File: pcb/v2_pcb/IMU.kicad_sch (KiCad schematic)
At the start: 13 parts, among them U1000 SCH16T-K01

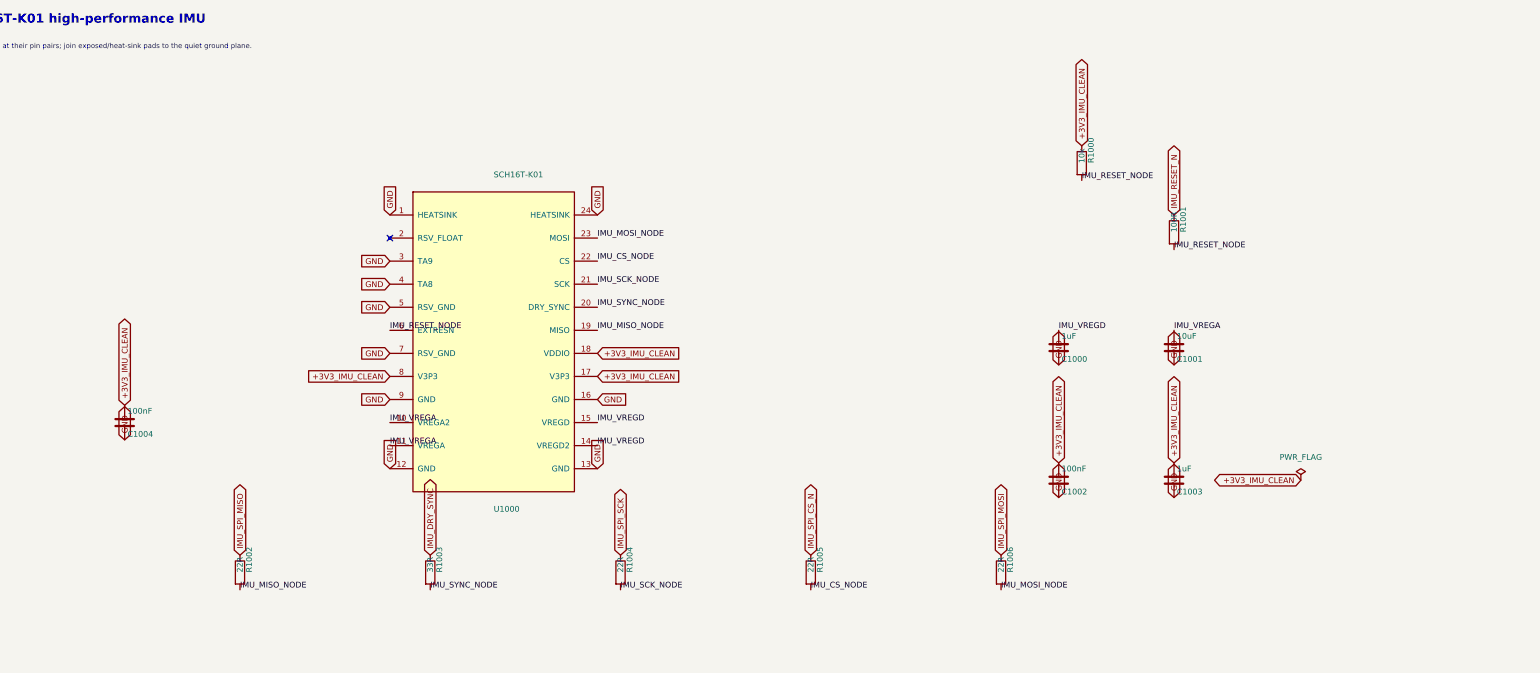
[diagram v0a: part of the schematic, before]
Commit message: switch mosfets
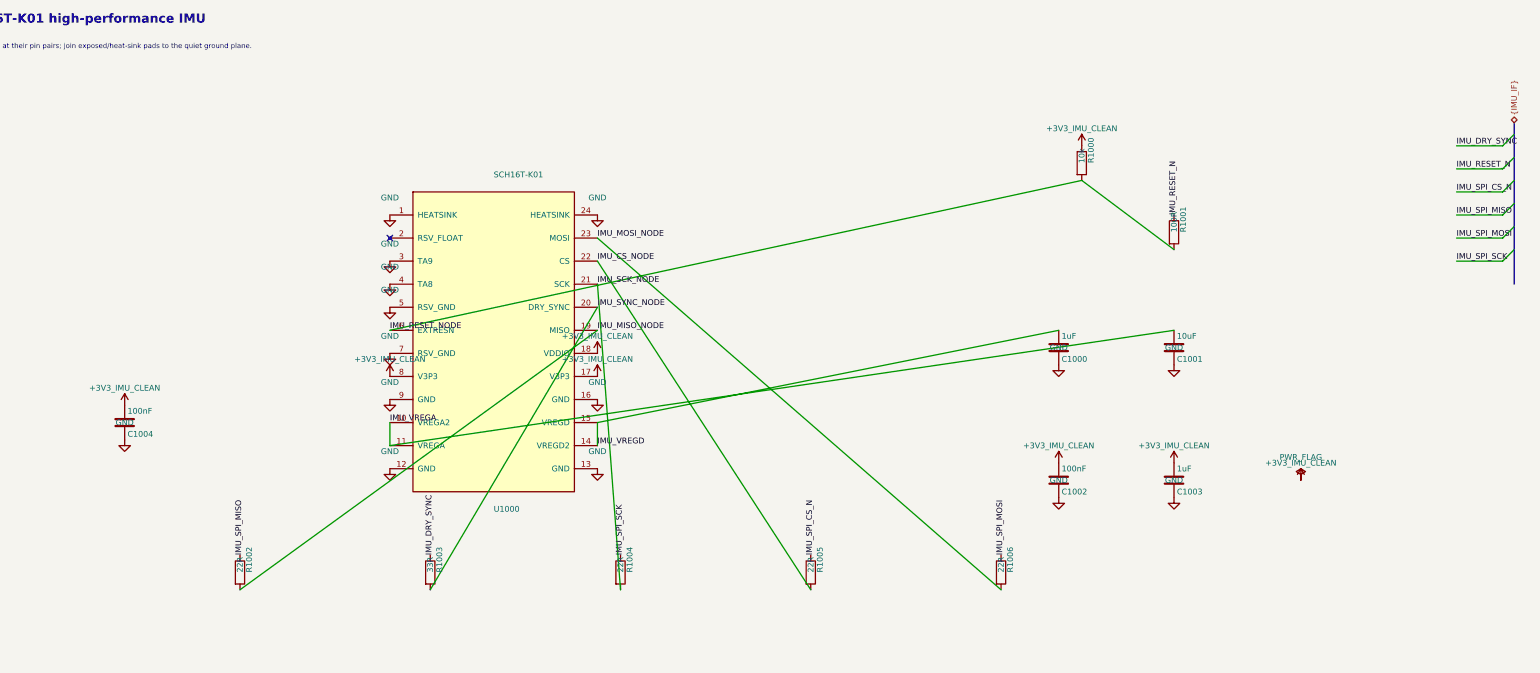
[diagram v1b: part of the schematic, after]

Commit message: clean pcb
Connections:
- net IMU_CS_NODE: no longer names the net of R1005.2, U1000.22 (CS)
- net IMU_MISO_NODE: no longer names the net of R1002.2, U1000.19 (MISO)
- net IMU_MOSI_NODE: no longer names the net of R1006.2, U1000.23 (MOSI)
- net IMU_RESET_NODE: no longer names the net of R1000.2, R1001.2, U1000.6 (EXTRESN)
- net IMU_SCK_NODE: no longer names the net of R1004.2, U1000.21 (SCK)
- net IMU_SYNC_NODE: no longer names the net of R1003.2, U1000.20 (DRY_SYNC)
- net IMU_VREGA: no longer names the net of C1001.1, U1000.10 (VREGA2), U1000.11 (VREGA)
- net IMU_VREGD: no longer names the net of C1000.1, U1000.14 (VREGD2), U1000.15 (VREGD)
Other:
- moved on the sheet: C1000, C1001, C1002, C1003, C1004, R1000, R1001, R1002, R1003, R1004, R1005, R1006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

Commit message: small
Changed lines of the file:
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@@
-	)
-	(junction
-		(at 175.26 127)
-		(diameter 0)
-		(color 0 0 0 0)
 	)
 	(junction
@@
 	)
 	(junction
+		(at 162.56 119.38)
+		(diameter 0)
+		(color 0 0 0 0)
+	)
+	(junction
 		(at 248.92 133.35)
 		(diameter 0)
@@
 	)
 	(junction
+		(at 162.56 127)
+		(diameter 0)
+		(color 0 0 0 0)
+	)
+	(junction
 		(at 191.77 113.03)
 		(diameter 0)
@@
 	(wire
 		(pts
+			(xy 168.91 113.03) (xy 182.88 113.03)
+		)
+		(stroke
+			(width 0)
+			(type default)
+		)
+	)
+	(wire
+		(pts
 			(xy 196.85 97.79) (xy 195.58 97.79)
 		)
@@
 	(wire
 		(pts
+			(xy 241.3 133.35) (xy 248.92 133.35)
+		)
+		(stroke
+			(width 0)
+			(type default)
+		)
+	)
+	(wire
+		(pts
+			(xy 337.82 76.2) (xy 347.98 76.2)
+		)
+		(stroke
+			(width 0)
+			(type default)
+		)
+	)
+	(wire
+		(pts
+			(xy 195.58 123.19) (xy 187.96 123.19)
+		)
+		(stroke
+			(width 0)
+			(type default)
+		)
+	)
+	(wire
+		(pts
+			(xy 256.54 119.38) (xy 267.97 119.38)
+		)
+		(stroke
+			(width 0)
+			(type default)
+		)
+	)
+	(wire
+		(pts
+			(xy 191.77 109.22) (xy 191.77 113.03)
+		)
+		(stroke
+			(width 0)
+			(type default)
+		)
+	)
+	(wire
+		(pts
+			(xy 195.58 133.35) (xy 187.96 133.35)
+		)
+		(stroke
+			(width 0)
+			(type default)
+		)
+	)
+	(wire
+		(pts
 			(xy 162.56 119.38) (xy 175.26 119.38)
-		)
-		(stroke
-			(width 0)
-			(type default)
-		)
-	)
-	(wire
-		(pts
-			(xy 241.3 133.35) (xy 248.92 133.35)
-		)
-		(stroke
-			(width 0)
-			(type default)
-		)
-	)
-	(wire
-		(pts
-			(xy 337.82 76.2) (xy 347.98 76.2)
-		)
-		(stroke
-			(width 0)
-			(type default)
-		)
-	)
-	(wire
-		(pts
-			(xy 195.58 123.19) (xy 187.96 123.19)
-		)
-		(stroke
-			(width 0)
-			(type default)
-		)
-	)
-	(wire
-		(pts
-			(xy 256.54 119.38) (xy 267.97 119.38)
-		)
-		(stroke
-			(width 0)
-			(type default)
-		)
-	)
-	(wire
-		(pts
-			(xy 191.77 109.22) (xy 191.77 113.03)
-		)
-		(stroke
-			(width 0)
-			(type default)
-		)
-	)
-	(wire
-		(pts
-			(xy 195.58 133.35) (xy 187.96 133.35)
 		)
 		(stroke
@@
 	)
 	(label "IMU_RESET_N"
-		(at 182.88 113.03 0)
+		(at 168.91 113.03 0)
 		(effects
 			(font
@@
 	(symbol
 		(lib_id "power:GND")
-		(at 175.26 127 0)
+		(at 162.56 127 0)
 		(unit 1)
 		(body_style 1)
@@
 		(fields_autoplaced yes)
 		(property "Reference" "#PWR00204"
-			(at 175.26 130.81 0)
+			(at 162.56 130.81 0)
 			(hide yes)
 			(show_name no)
@@
 		)
 		(property "Value" "GND"
-			(at 177.8 128.2699 0)
+			(at 165.1 128.2699 0)
 			(show_name no)
 			(do_not_autoplace no)
@@
 		)
 		(property "Footprint" ""
-			(at 175.26 127 0)
+			(at 162.56 127 0)
 			(hide yes)
 			(show_name no)
@@
 		)
 		(property "Datasheet" ""
-			(at 175.26 127 0)
+			(at 162.56 127 0)
 			(hide yes)
 			(show_name no)
@@
 		)
 		(property "Description" "Power symbol creates a global label with name \"GND\""
-			(at 175.26 127 0)
+			(at 162.56 127 0)
 			(hide yes)
 			(show_name no)
@@
 	(symbol
 		(lib_id "power:+3V3")
-		(at 175.26 119.38 0)
+		(at 162.56 119.38 0)
 		(unit 1)
 		(body_style 1)
@@
 		(fields_autoplaced yes)
 		(property "Reference" "#PWR00203"
-			(at 175.26 123.19 0)
+			(at 162.56 123.19 0)
 			(hide yes)
 			(show_name no)
@@
 		)
 		(property "Value" "+3V3_IMU_CLEAN"
-			(at 175.26 115.57 0)
+			(at 162.56 115.57 0)
 			(show_name no)
 			(do_not_autoplace no)
@@
 		)
 		(property "Footprint" ""
-			(at 175.26 119.38 0)
+			(at 162.56 119.38 0)
 			(hide yes)
 			(show_name no)
@@
 		)
 		(property "Datasheet" ""
-			(at 175.26 119.38 0)
+			(at 162.56 119.38 0)
 			(hide yes)
 			(show_name no)
@@
 		)
 		(property "Description" "Power symbol creates a global label with name \"+3V3_IMU_CLEAN\""
-			(at 175.26 119.38 0)
+			(at 162.56 119.38 0)
 			(hide yes)
 			(show_name no)
@@
 		)
 	)
-	(embedded_fonts no)
 )

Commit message: minor fixes
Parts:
- C1000, C1003: value 1uF -> 1uF 25V X7R; Dielectric (none) -> X7R; MPN (none) -> CGA3E1X7R1E105K080AE; Manufacturer (none) -> TDK; Qualification (none) -> AEC-Q200; Termination (none) -> Soft termination; Tolerance (none) -> ±10%; Voltage (none) -> 25 VDC
- C1001: value 10uF -> 10uF 10V X7R; Dielectric (none) -> X7R; MPN (none) -> GCJ21BR71A106KE01L; Manufacturer (none) -> Murata; Qualification (none) -> AEC-Q200; Termination (none) -> Soft termination; Tolerance (none) -> ±10%; Voltage (none) -> 10 VDC
- C1002, C1004: value 100nF -> 100nF 50V X7R; Dielectric (none) -> X7R; MPN (none) -> CGA2B3X7R1H104K050BE; Manufacturer (none) -> TDK; Qualification (none) -> AEC-Q200; Termination (none) -> Soft termination; Tolerance (none) -> ±10%; Voltage (none) -> 50 VDC
- R1000: MPN (none) -> CRCW040210K0FKED; Manufacturer (none) -> Vishay; Power (none) -> 0.063 W; TCR (none) -> ±100 ppm/K; Tolerance (none) -> ±1%
- R1001: MPN (none) -> CRCW0402100RFKED; Manufacturer (none) -> Vishay; Power (none) -> 0.063 W; TCR (none) -> ±100 ppm/K; Tolerance (none) -> ±1%
- R1002, R1004, R1005, R1006: MPN (none) -> CRCW040222R0FKED; Manufacturer (none) -> Vishay; Power (none) -> 0.063 W; TCR (none) -> ±100 ppm/K; Tolerance (none) -> ±1%
- R1003: MPN (none) -> CRCW040233R0FKED; Manufacturer (none) -> Vishay; Power (none) -> 0.063 W; TCR (none) -> ±100 ppm/K; Tolerance (none) -> ±1%
- U1000: value SCH16T-K01 -> SCH16T-K01-1; MPN SCH16T-K01 -> SCH16T-K01-1; Manufacturer Murata Electronics -> Murata; Packing (none) -> 100-piece tape/reel; Release_Status (none) -> Obtain controlled full SCH16T-K01 datasheet/approval sheet 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
